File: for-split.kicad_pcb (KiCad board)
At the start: 2 copper layers, 114.3 x 95.3 mm, 75 parts, among them J1 TRRS, J2 TRRS, U1 ProMicro

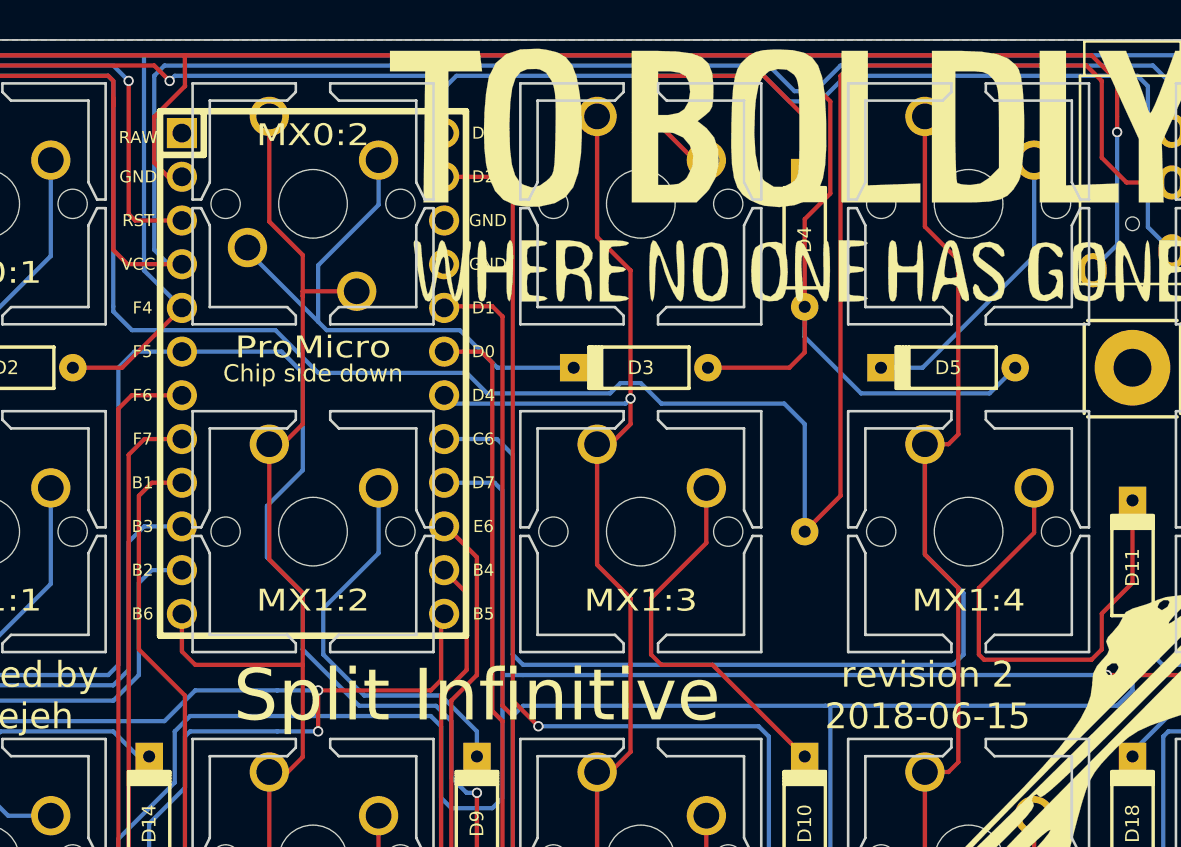
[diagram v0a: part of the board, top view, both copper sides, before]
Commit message: Add zigzag Pro Micro footprint
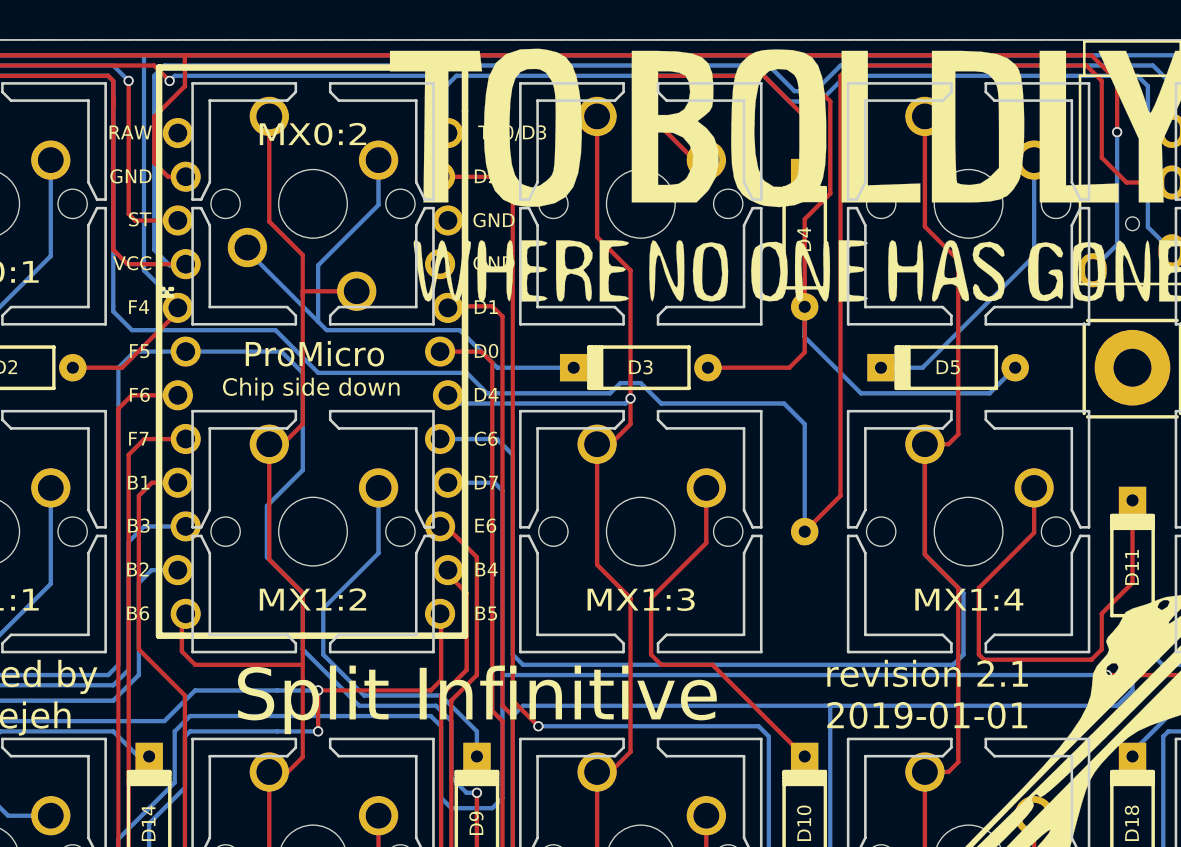
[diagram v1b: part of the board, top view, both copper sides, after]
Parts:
- U1: footprint idle-hands:Pro_Micro_ChipSideDown -> idle-hands:Pro_Micro_ZigZag
- moved U1 1.55 mm to (155.2, 83.7)
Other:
- board text added: "revision 2.1 2019-01-01"
- board text removed: "revision 2 2018-06-15"
